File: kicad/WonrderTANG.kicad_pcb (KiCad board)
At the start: 2 copper layers, 101.6 x 90.2 mm, 30 parts, among them CON1 MSX-CONNECTOR, J2 AudioJack3, J3 Conn_02x03_Odd_Even, U1 SN74LVC245AN, U2 SN74LVC245AN, U3 SN74LVC245AN, U4 MCP6281, U5 SN74LVC245AN, U6 Tang_Nano_20k, U7 SN74LVC245AN

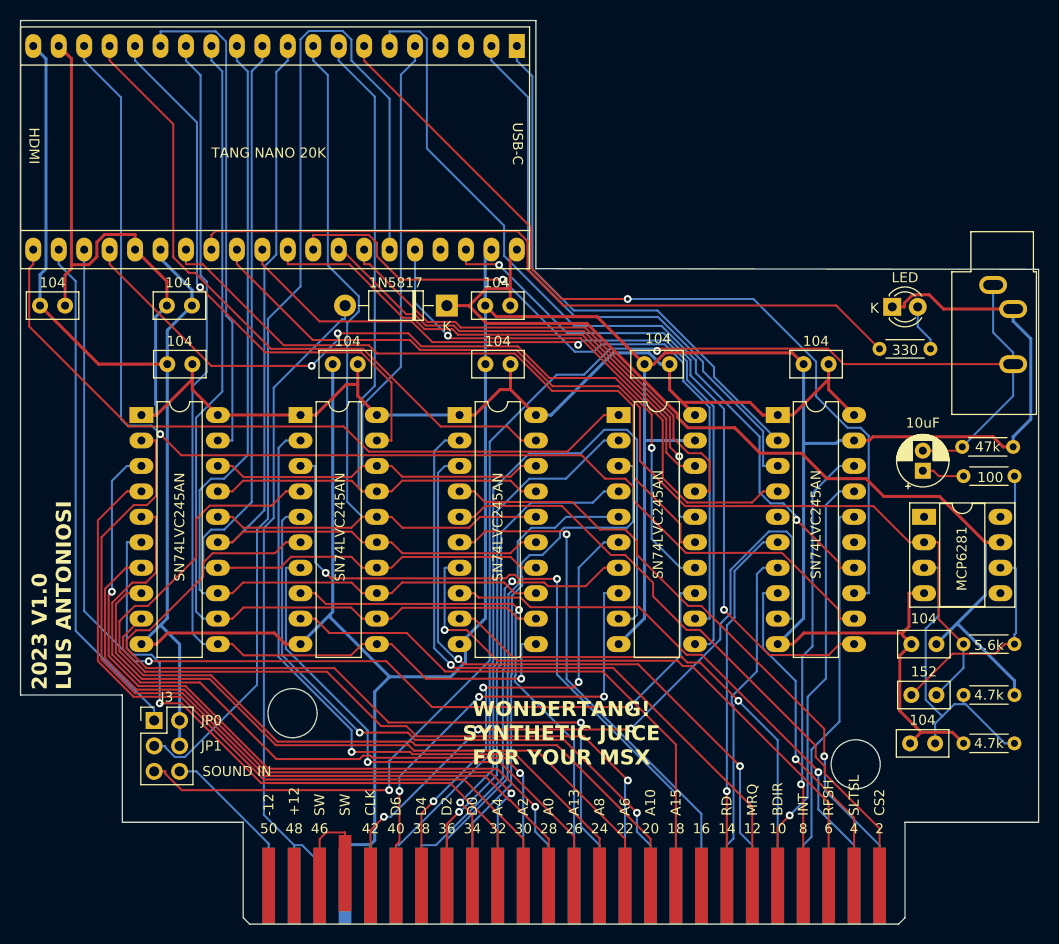
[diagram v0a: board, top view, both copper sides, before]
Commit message: fix on wait line
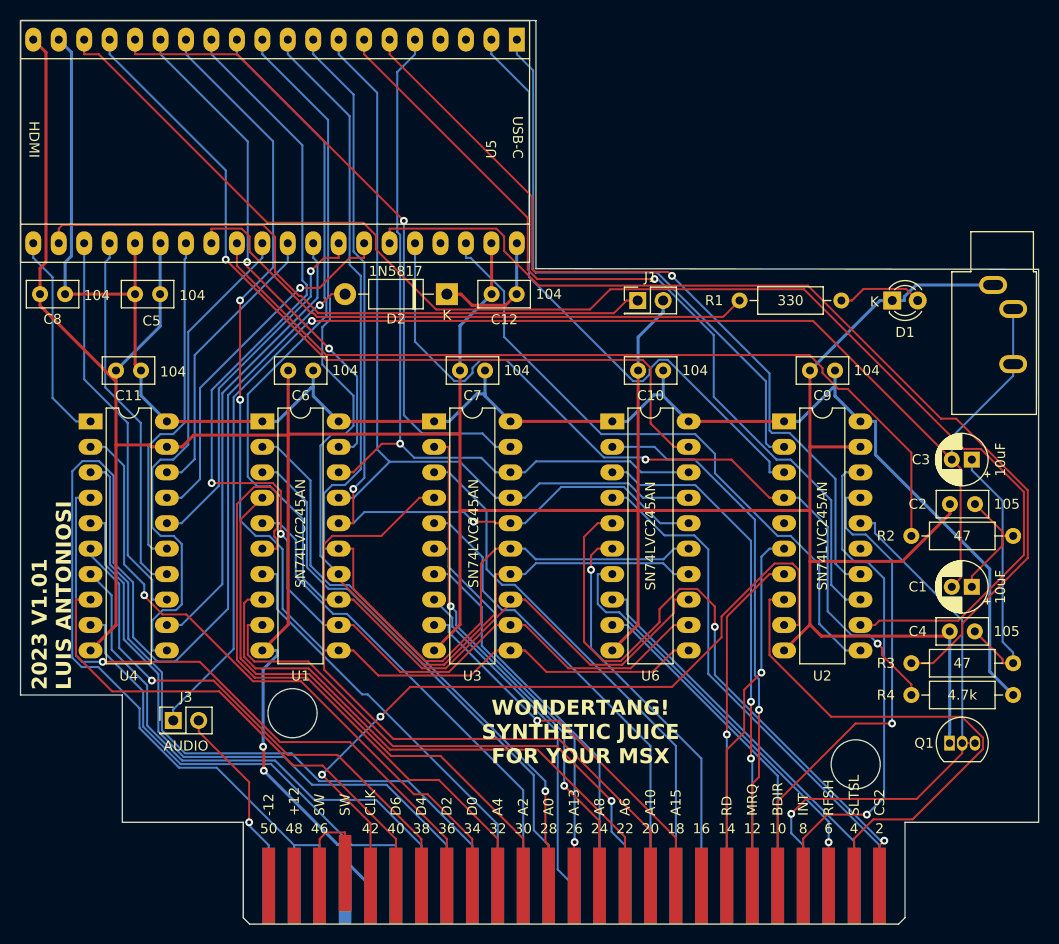
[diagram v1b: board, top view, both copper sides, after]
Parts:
- removed R5: 4.7k, Resistor_THT:R_Axial_DIN0204_L3.6mm_D1.6mm_P5.08mm_Horizontal
- removed R6: 47k, Resistor_THT:R_Axial_DIN0204_L3.6mm_D1.6mm_P5.08mm_Horizontal
- removed U7: SN74LVC245AN, Package_DIP:DIP-20_W7.62mm_LongPads
- added J1: Conn_02x01, Connector_PinHeader_2.54mm:PinHeader_2x01_P2.54mm_Vertical, F.Cu at (118.1, 81.3)
- added Q1: 2N3904, Package_TO_SOT_THT:TO-92_Inline, F.Cu at (149.2, 125.5)
- C1: value 152 -> 10uF; footprint Capacitor_THT:C_Disc_D5.0mm_W2.5mm_P2.50mm -> Capacitor_THT:CP_Radial_D5.0mm_P2.00mm
- C2: value 10uF -> 105; footprint Capacitor_THT:CP_Radial_D5.0mm_P2.00mm -> Capacitor_THT:C_Disc_D5.0mm_W2.5mm_P2.50mm
- C3: value 104 -> 10uF; footprint Capacitor_THT:C_Disc_D5.0mm_W2.5mm_P2.50mm -> Capacitor_THT:CP_Radial_D5.0mm_P2.00mm
- C4: value 104 -> 105
- J3: value Conn_02x03_Odd_Even -> Conn_02x01; footprint Connector_PinHeader_2.54mm:PinHeader_2x03_P2.54mm_Vertical -> Connector_PinHeader_2.54mm:PinHeader_2x01_P2.54mm_Vertical
- R1: footprint Resistor_THT:R_Axial_DIN0204_L3.6mm_D1.6mm_P5.08mm_Horizontal -> Resistor_THT:R_Axial_DIN0207_L6.3mm_D2.5mm_P10.16mm_Horizontal
- R2: value 5.6k -> 47; footprint Resistor_THT:R_Axial_DIN0204_L3.6mm_D1.6mm_P5.08mm_Horizontal -> Resistor_THT:R_Axial_DIN0207_L6.3mm_D2.5mm_P10.16mm_Horizontal
- R3: value 4.7k -> 47; footprint Resistor_THT:R_Axial_DIN0204_L3.6mm_D1.6mm_P5.08mm_Horizontal -> Resistor_THT:R_Axial_DIN0207_L6.3mm_D2.5mm_P10.16mm_Horizontal
- R4: value 100 -> 4.7k; footprint Resistor_THT:R_Axial_DIN0204_L3.6mm_D1.6mm_P5.08mm_Horizontal -> Resistor_THT:R_Axial_DIN0207_L6.3mm_D2.5mm_P10.16mm_Horizontal
- U4: value MCP6281 -> SN74LVC245AN; footprint Package_DIP:DIP-8_W7.62mm_Socket_LongPads -> Package_DIP:DIP-20_W7.62mm_LongPads
- U5: value SN74LVC245AN -> Tang_Nano_20k; footprint Package_DIP:DIP-20_W7.62mm_LongPads -> Mis_huellas:Tang_Nano_20k
- U6: value Tang_Nano_20k -> SN74LVC245AN; footprint Mis_huellas:Tang_Nano_20k -> Package_DIP:DIP-20_W7.62mm_LongPads
- moved U4 83.7 mm to (63.5, 93.3)
- moved C12 54.5 mm to (106.0, 80.6)
- moved C4 40.5 mm to (151.7, 114.3)
- moved U5 38.8 mm to (106.0, 55.2), turned to -90 degrees
- moved U6 38.7 mm to (115.6, 93.3), turned to 0 degrees
- moved C11 37.4 mm to (68.5, 88.3)
- moved C9 32.4 mm to (137.8, 88.3)
- moved C3 28.6 mm to (151.5, 97.2)
- moved R4 21.8 mm to (155.6, 120.7)
- moved C10 16.5 mm to (120.7, 88.3)
- moved R1 14.8 mm to (128.3, 81.3)
- moved U3 13.4 mm to (97.8, 93.3)
- moved C7 12.7 mm to (102.9, 88.3)
- moved C6 12.1 mm to (85.7, 88.3)
- moved U1 12.1 mm to (80.6, 93.3)
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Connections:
- C1 pad 1: SOUND_33 -> Net-(C1-Pad1)
- C1 pad 2: Net-(C1-Pad2) -> /AUDIO
- C11 pad 1: +5V -> +3.3V
- C2 pad 1: Net-(C2-Pad1) -> Net-(C1-Pad1)
- C2 pad 2: SOUNDOUT -> GND
- C3 pad 1: Net-(U4-+) -> Net-(C3-Pad1)
- C3 pad 2: GND -> /AUDIO
- C4 pad 1: +3.3V -> Net-(C3-Pad1)
- J2 pad R: SOUNDOUT -> /AUDIO
- J2 pad S: SOUNDOUT -> GND
- J2 pad T: GND -> /AUDIO
- J3 pad 1: JP0 -> /AUDIO
- J3 pad 2: GND -> SOUNDIN
- R2 pad 2: Net-(C1-Pad2) -> Net-(C1-Pad1)
- R3 pad 1: Net-(U4-+) -> AUDIO_33
- R3 pad 2: +5V -> Net-(C3-Pad1)
- R4 pad 1: Net-(C1-Pad2) -> +3.3V
- R4 pad 2: Net-(C2-Pad1) -> WAIT_33
- U4 pad 1: unconnected-(U4-NC-Pad1) -> DATADIR
- U4 pad 2: SOUND_33 -> D0
- U4 pad 3: Net-(U4-+) -> D1
- U4 pad 4: GND -> D2
- U4 pad 5: unconnected-(U4-NC-Pad5) -> D3
- U4 pad 6: Net-(C1-Pad2) -> D4
- U4 pad 7: +5V -> D5
- U4 pad 8: unconnected-(U4-NC-Pad8) -> D6
- U5 pad 1: DATADIR -> INT_33
- U5 pad 10: GND -> MP3_33
- U5 pad 11: D7_33 -> MP4_33
- U5 pad 12: D6_33 -> MP5_33
- U5 pad 13: D5_33 -> MP6_33
- U5 pad 14: D4_33 -> MP7_33
- U5 pad 15: D3_33 -> MSEL0_33
- U5 pad 16: D2_33 -> MSEL1_33
- U5 pad 17: D1_33 -> MSEL2_33
- U5 pad 18: D0_33 -> SLTSL_33
- U5 pad 19: GND -> +3.3V
- U5 pad 2: D0 -> BUSDIR_33
- U5 pad 20: +3.3V -> GND
- U5 pad 3: D1 -> unconnected-(U5-75_IOT34A-Pad3)
- U5 pad 4: D2 -> unconnected-(U5-85_IOT4B-Pad4)
- U5 pad 5: D3 -> MP0_33
- U5 pad 6: D4 -> RD_33
- U5 pad 7: D5 -> WR_33
- U5 pad 8: D6 -> MP1_33
- U5 pad 9: D7 -> MP2_33
- U6 pad 1: INT_33 -> +3.3V
- U6 pad 10: MP3_33 -> GND
- U6 pad 11: MP4_33 -> MP7_33
- U6 pad 12: MP5_33 -> MP6_33
- U6 pad 13: MP6_33 -> MP5_33
- U6 pad 14: MP7_33 -> MP4_33
- U6 pad 15: MSEL0_33 -> MP3_33
- U6 pad 16: MSEL1_33 -> MP2_33
- U6 pad 17: MSEL2_33 -> MP1_33
- U6 pad 18: SLTSL_33 -> MP0_33
- U6 pad 19: +3.3V -> MSEL2_33
- U6 pad 2: BUSDIR_33 -> MERQ
- U6 pad 20: GND -> +3.3V
- U6 pad 3: unconnected-(U6-75_IOT34A-Pad3) -> IORQ
- U6 pad 4: unconnected-(U6-85_IOT4B-Pad4) -> CS1
- U6 pad 5: MP0_33 -> CS2
- U6 pad 6: RD_33 -> RESET
- U6 pad 7: WR_33 -> RFSH
- U6 pad 8: MP1_33 -> CS12
- U6 pad 9: MP2_33 -> M1
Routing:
- net /AUDIO: track 0.00 -> 146.3 mm, vias 0 -> 1
- net SOUNDOUT: track 143.4 -> 0.00 mm, vias 2 -> 0
- net JP1: track 108.3 -> 0.00 mm
- net AUDIO_33: track 0.00 -> 100.1 mm
- net +5V: track 99.1 -> 13.0 mm
- net D5_33: track 109.4 -> 39.8 mm, vias 2 -> 0
- net JP: track 0.00 -> 65.6 mm
- net Net-(CON1-5V@1): track 68.3 -> 132.2 mm, vias 0 -> 1
- net DATADIR: track 73.4 -> 21.0 mm
- net JP0: track 50.9 -> 0.00 mm
- net A12: track 88.5 -> 41.3 mm, vias 1 -> 0
- net D4_33: track 82.8 -> 36.6 mm, vias 3 -> 0
- net D3_33: track 69.0 -> 34.4 mm
- net D7: track 80.4 -> 47.4 mm
- net Net-(C1-Pad2): track 30.7 -> 0.00 mm
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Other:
- board text added: "2023 V1.01 LUIS ANTONIOSI"
- board text removed: "2023 V1.0 LUIS ANTONIOSI"

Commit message: kicad final version 1.01
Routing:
- net Net-(CON1-5V@1): track 132.2 -> 74.1 mm, vias 1 -> 2
- net /AUDIO: track 146.3 -> 188.9 mm
- net A15: track 38.1 -> 67.5 mm, vias 1 -> 0
- net SLTSL_33: track 141.3 -> 114.3 mm, vias 0 -> 2
- net SLTSL: track 54.1 -> 31.5 mm, vias 0 -> 1
- net MSEL0_33: track 50.4 -> 72.2 mm
- net MP0_33: track 79.4 -> 100.9 mm
- net A8: track 51.5 -> 69.3 mm, vias 2 -> 0
- net CS2: track 67.5 -> 51.9 mm, vias 2 -> 1
- net A4: track 65.9 -> 50.3 mm
- net MP3_33: track 108.4 -> 96.4 mm, vias 0 -> 1
- net MP5_33: track 115.2 -> 126.0 mm
- net GND: track 392.0 -> 401.0 mm, vias 2 -> 1
- net MP4_33: track 106.5 -> 113.9 mm, vias 0 -> 2
- net D4: track 53.8 -> 61.0 mm, vias 1 -> 0
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
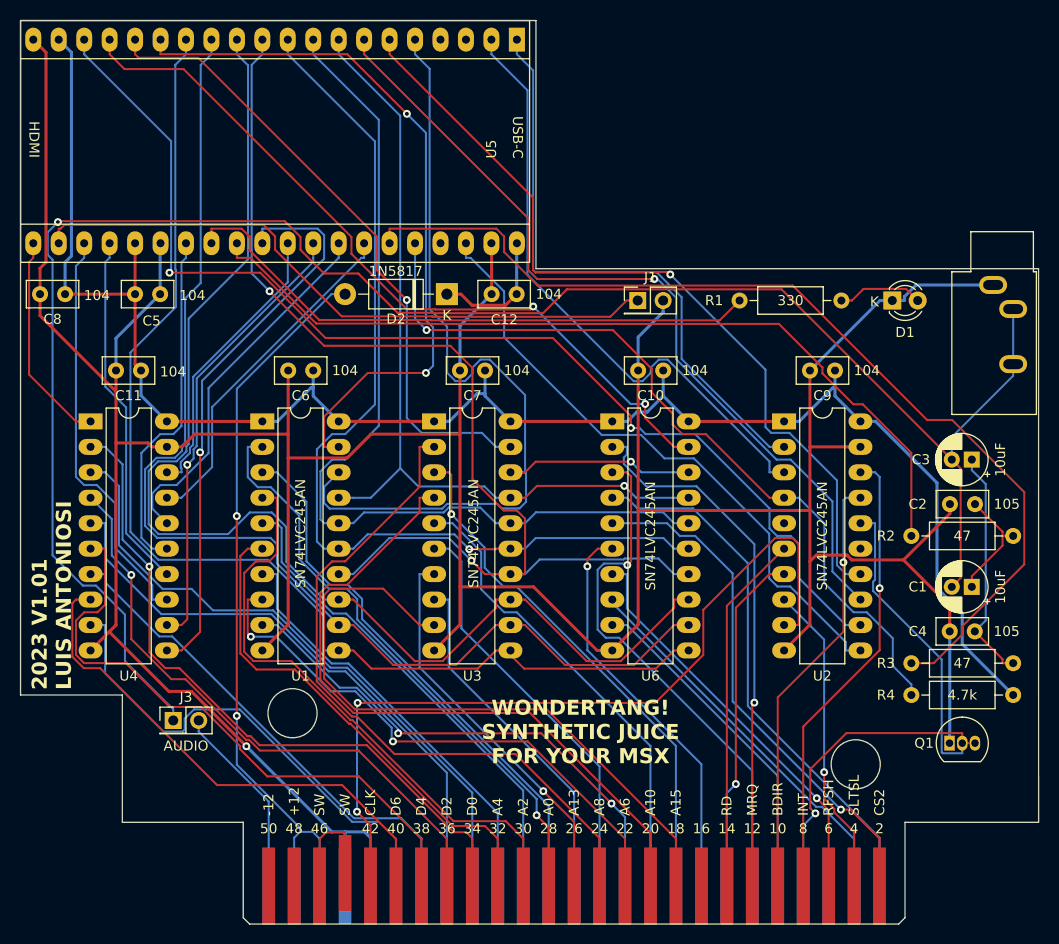
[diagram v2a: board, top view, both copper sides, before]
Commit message: kicad fixes
fix shorted transistor add 10uf power line, moved cap to allow be placed horizontally
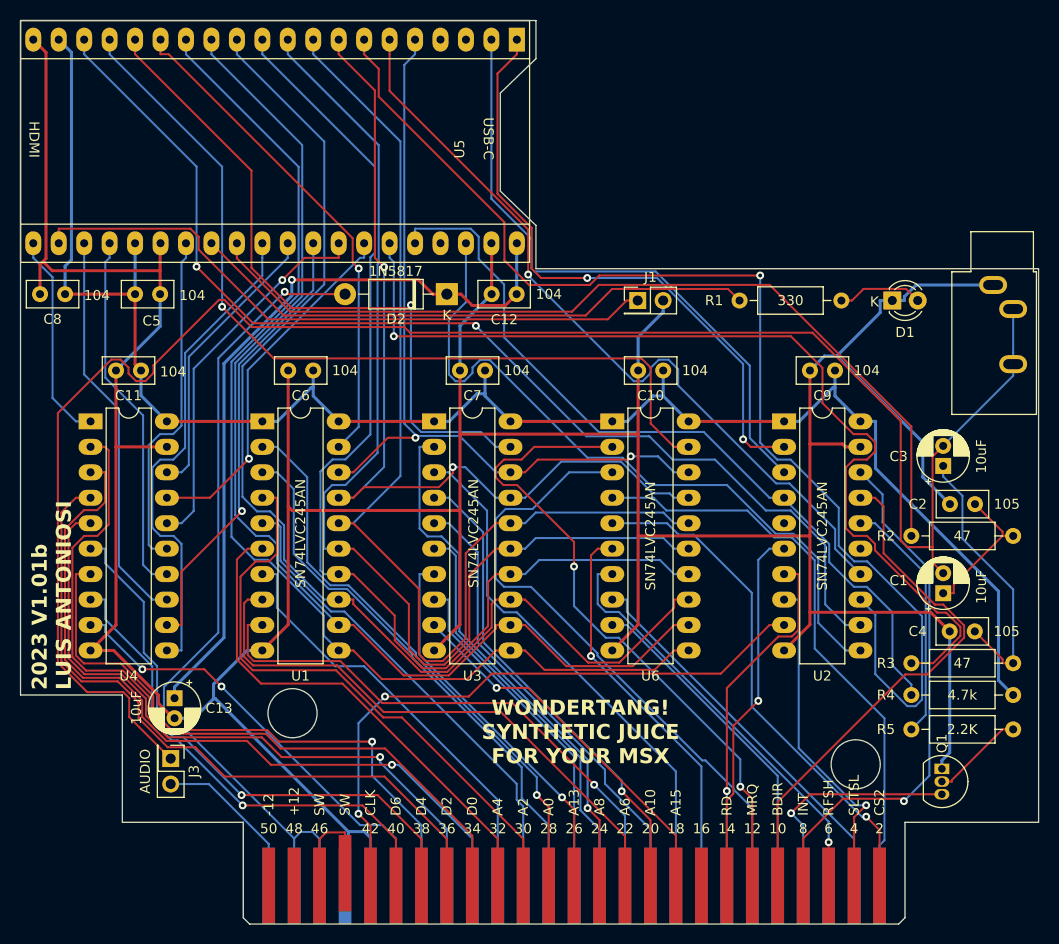
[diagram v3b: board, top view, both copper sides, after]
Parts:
- added C13: 10uF, Capacitor_THT:CP_Radial_D5.0mm_P2.00mm, F.Cu at (71.9, 121.0)
- added R5: 2.2K, Resistor_THT:R_Axial_DIN0207_L6.3mm_D2.5mm_P10.16mm_Horizontal, F.Cu at (145.4, 124.1)
- moved J3 3.81 mm to (71.5, 127.0), turned to -90 degrees
- moved C3 2.93 mm to (148.6, 97.8), turned to 90 degrees
- moved C1 2.93 mm to (148.6, 110.5), turned to 90 degrees
- moved Q1 2.67 mm to (148.5, 128.0), turned to -90 degrees
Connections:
- Q1 pad 2: WAIT -> Net-(Q1-B)
- U2 pad 16: WAIT -> /WAIT_SW
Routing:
- net +5V: track 13.0 -> 75.7 mm, vias 0 -> 1
- net WAIT: track 61.6 -> 23.6 mm
- net WR_33: track 84.3 -> 119.6 mm
- net A15: track 67.5 -> 37.9 mm, vias 0 -> 1
- net /WAIT_SW: track 0.00 -> 24.7 mm
- net MSEL0_33: track 72.2 -> 50.1 mm, vias 2 -> 1
- net MP0_33: track 100.9 -> 79.8 mm, vias 1 -> 2
- net A10: track 69.4 -> 48.5 mm, vias 0 -> 1
- net CLOCK: track 82.1 -> 63.3 mm
- net MP2_33: track 92.9 -> 111.3 mm
- net A8: track 69.3 -> 53.5 mm, vias 0 -> 1
- net MP3_33: track 96.4 -> 110.8 mm, vias 1 -> 0
- net MERQ: track 53.8 -> 66.4 mm, vias 1 -> 2
- net D1: track 64.1 -> 76.3 mm, vias 0 -> 1
- net D5: track 49.2 -> 60.1 mm, vias 0 -> 1
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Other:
- outline, holes or cut-outs redrawn
- board text added: "2023 V1.01b LUIS ANTONIOSI"
- board text removed: "2023 V1.01 LUIS ANTONIOSI"

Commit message: Fix board audio
audio pins were connected together
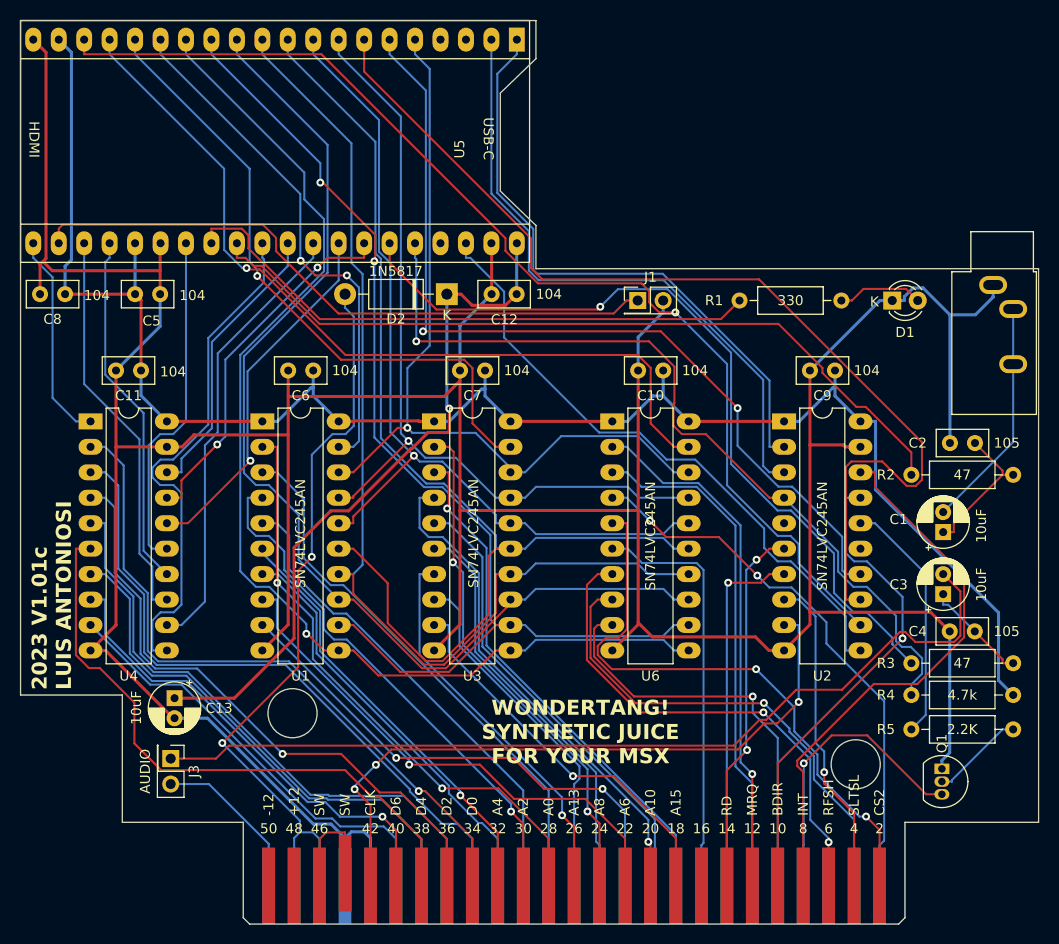
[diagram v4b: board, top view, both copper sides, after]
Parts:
- moved C3 12.8 mm to (148.6, 110.6)
- moved R2 6.10 mm to (145.4, 98.7)
- moved C1 6.10 mm to (148.6, 104.4)
- moved C2 6.10 mm to (151.8, 95.5)
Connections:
- C1 pad 2: /AUDIO -> Net-(C1-Pad2)
- C3 pad 2: /AUDIO -> Net-(J3-Pin_1)
- J2 pad R: /AUDIO -> Net-(C1-Pad2)
- J2 pad T: /AUDIO -> Net-(C1-Pad2)
- J3 pad 1: /AUDIO -> Net-(J3-Pin_1)
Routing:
- net /AUDIO: track 183.1 -> 0.00 mm
- net Net-(J3-Pin_1): track 0.00 -> 91.6 mm
- net MP2_33: track 111.3 -> 88.0 mm, vias 0 -> 1
- net Net-(C1-Pad2): track 0.00 -> 23.2 mm
- net Net-(C3-Pad1): track 28.0 -> 10.7 mm
- net WR_33: track 119.6 -> 103.4 mm, vias 1 -> 0
- net AUDIO_33: track 97.3 -> 81.4 mm
- net MERQ: track 66.4 -> 52.5 mm, vias 2 -> 1
- net IORQ: track 62.6 -> 51.1 mm
- net D1: track 76.3 -> 66.3 mm, vias 1 -> 0
- net RD_33: track 79.0 -> 88.6 mm, vias 1 -> 2
- net D0: track 78.1 -> 68.5 mm, vias 0 -> 1
- net SOUND_33: track 88.9 -> 79.3 mm
- net CS12: track 39.4 -> 48.8 mm, vias 0 -> 1
- net CLOCK_33: track 72.1 -> 62.9 mm
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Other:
- board text added: "2023 V1.01c LUIS ANTONIOSI"
- board text removed: "2023 V1.01b LUIS ANTONIOSI"
